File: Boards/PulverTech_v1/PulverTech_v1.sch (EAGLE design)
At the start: 40 parts, among them IC1 786TV, K1 G5LE, P1 FSMCD, Q1 16.0 mHz, Q10 BC548, Q2 BC548, Q3 BC548, Q4 BC548, Q6 IRF540, Q7 IRF540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

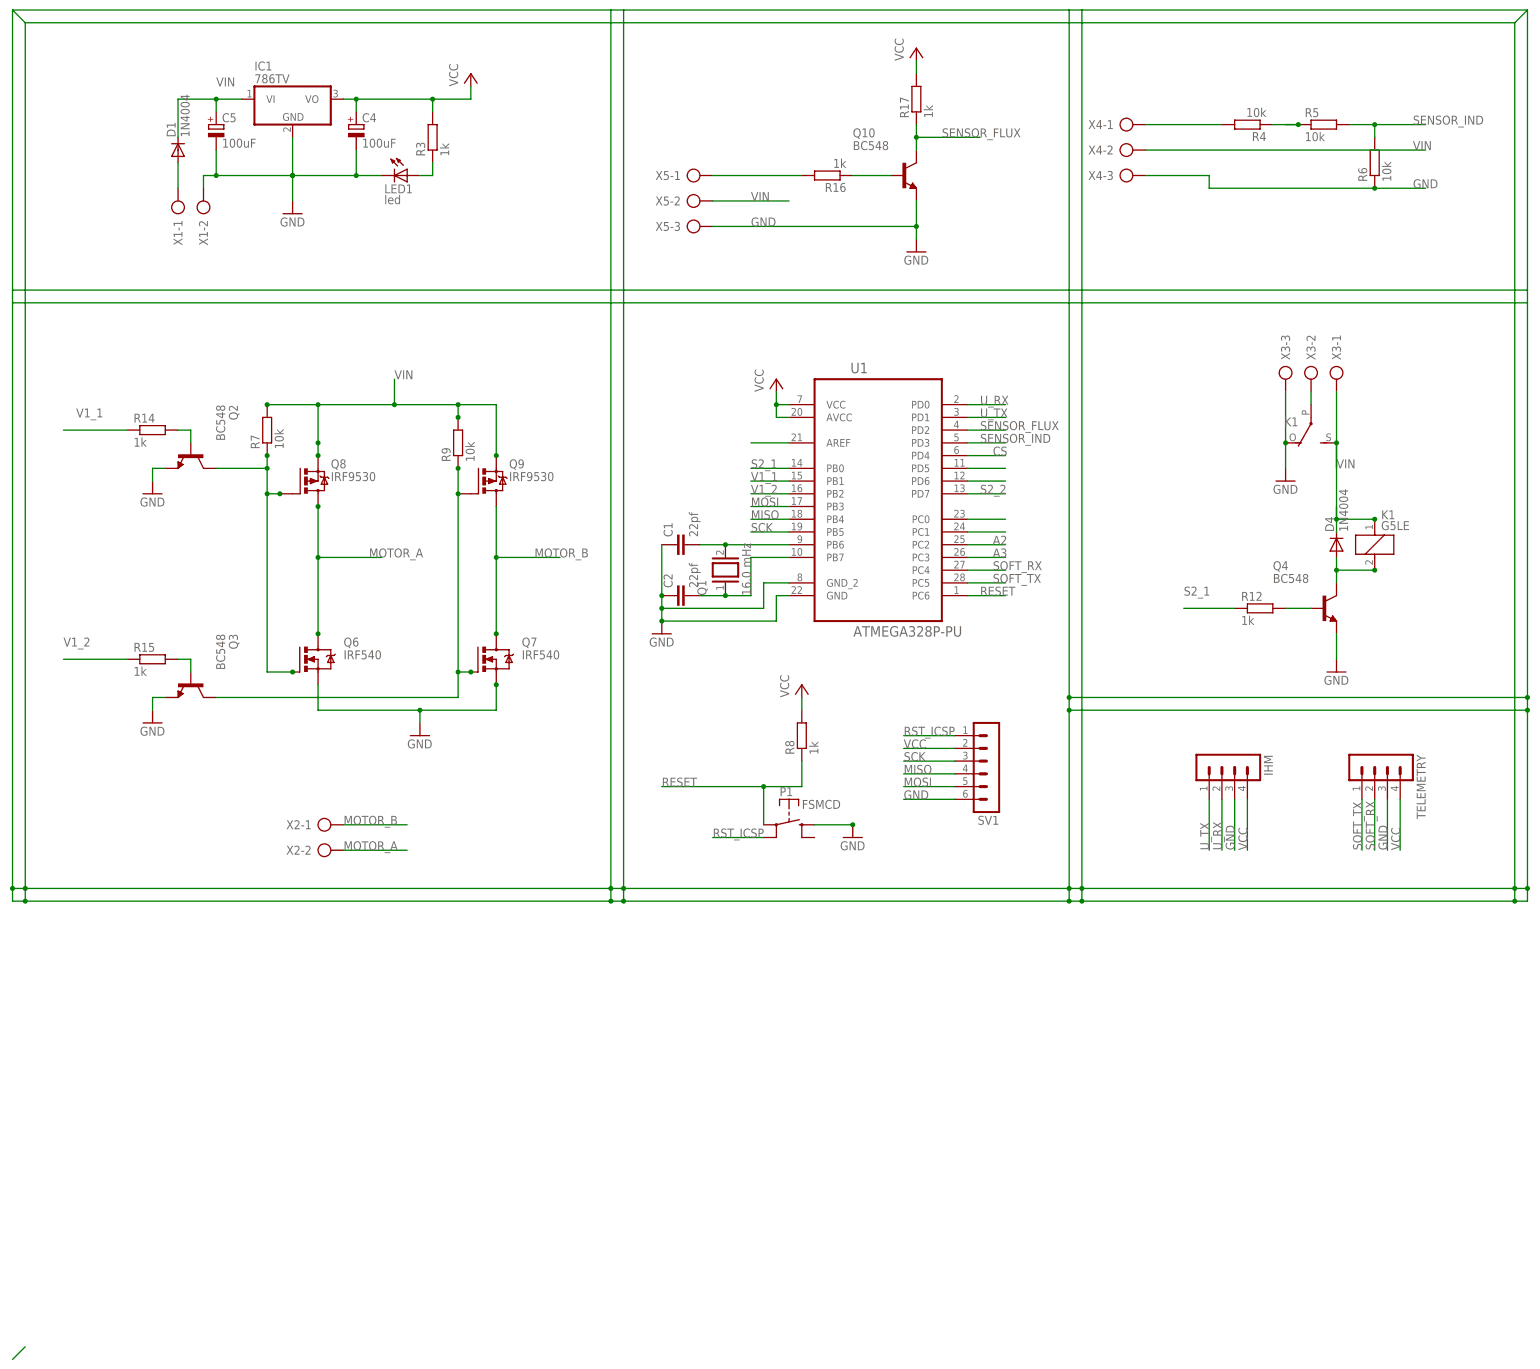
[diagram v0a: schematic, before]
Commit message: Add optocouplers, changed sensor input for flux and minor changes
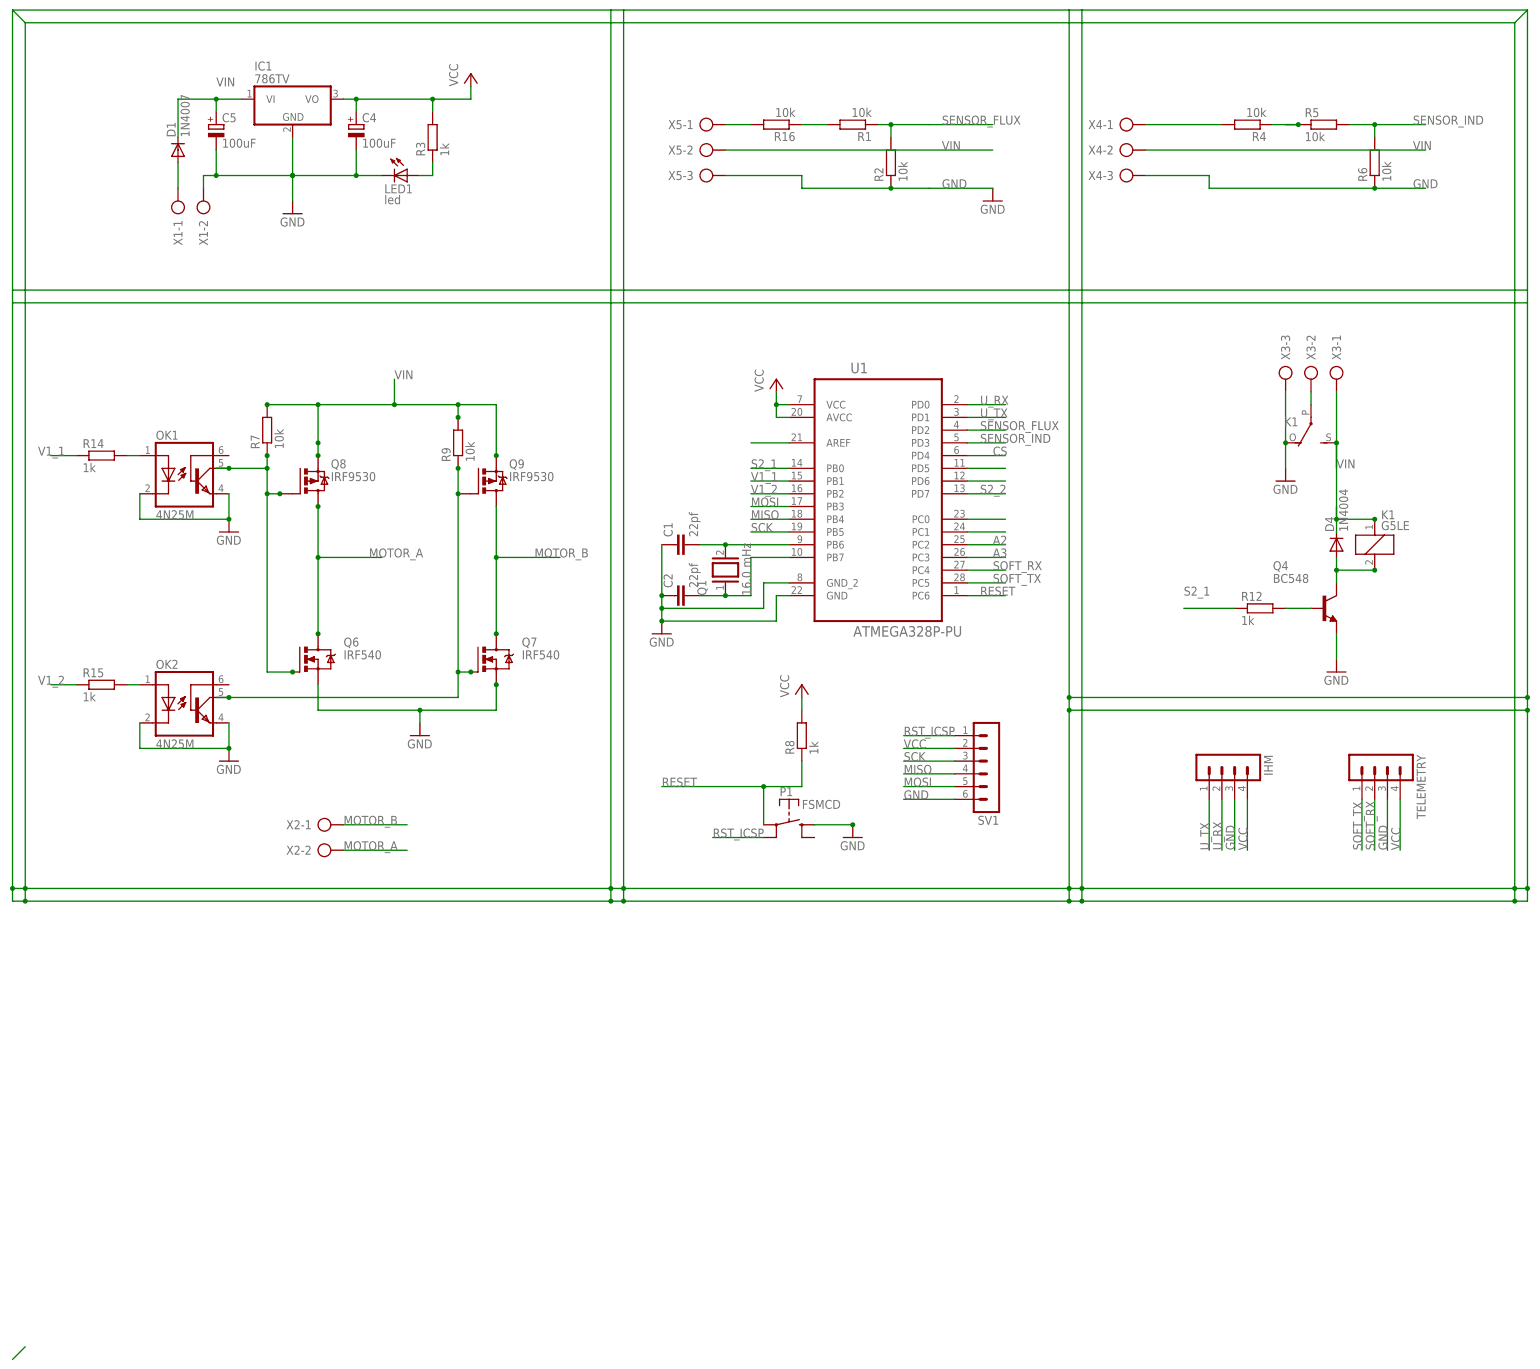
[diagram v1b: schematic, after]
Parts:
- removed Q10, Q2, Q3: BC548, transistor-npn:BC548
- removed R17: 1k, eagle-ltspice:R0204/7
- added OK1, OK2: 4N25M, optocoupler:4N25M
- added R1, R2: 10k, eagle-ltspice:R0204/7
- D1: value 1N4004 -> 1N4007
- R16: value 1k -> 10k
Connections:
- removed net N$38: Q2.C, Q6.G, Q8.G, R7.1
- removed net N$7: Q3.B, R15.2
- new net N$16: OK1.A, R14.2
- new net N$17: OK2.A, R15.2
- net GND: now also OK1.C, OK1.EMI, OK2.C, OK2.EMI, R2.1; no longer Q10.E, Q2.E, Q3.E
- net N$15: now also OK1.COL, Q6.G, Q8.G, R7.1; no longer Q2.B, R14.2
- net N$39: now also OK2.COL; no longer Q3.C
- net N$4: now also R1.2; no longer Q10.B
- net SENSOR_FLUX: now also R1.1, R2.2; no longer Q10.C, R17.1
- net VCC: no longer R17.2
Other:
- moved on the sheet: R14, R15, R16, X5-1, X5-2, X5-3
